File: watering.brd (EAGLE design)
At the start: 84.8 x 64.8 mm, 36 parts, among them IC1 LM324N, IC2 7805T, J1 DCJ0202, Q1 IRF510, T1 2N2222, T2 2N2222, T3 2N2222

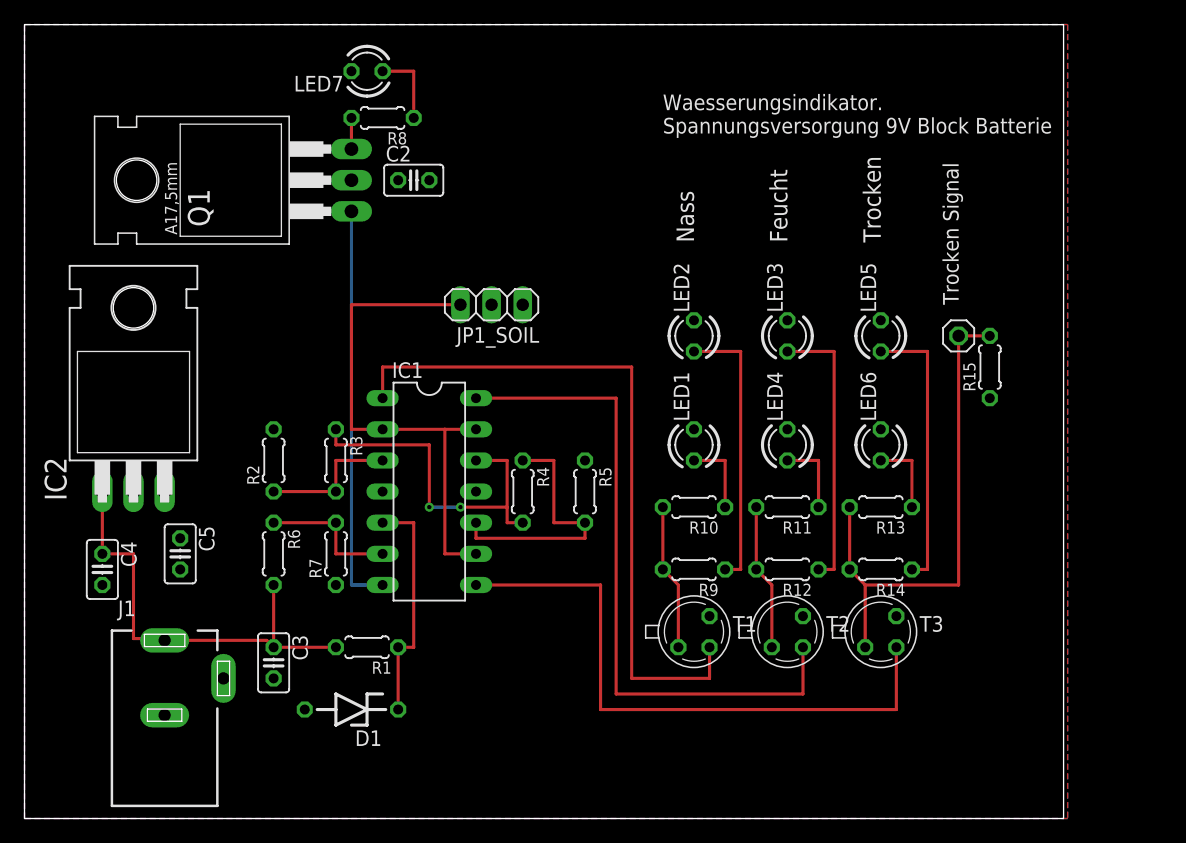
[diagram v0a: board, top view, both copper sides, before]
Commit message: Remove LED labels and reorganised battery indicator to shrinken the design.
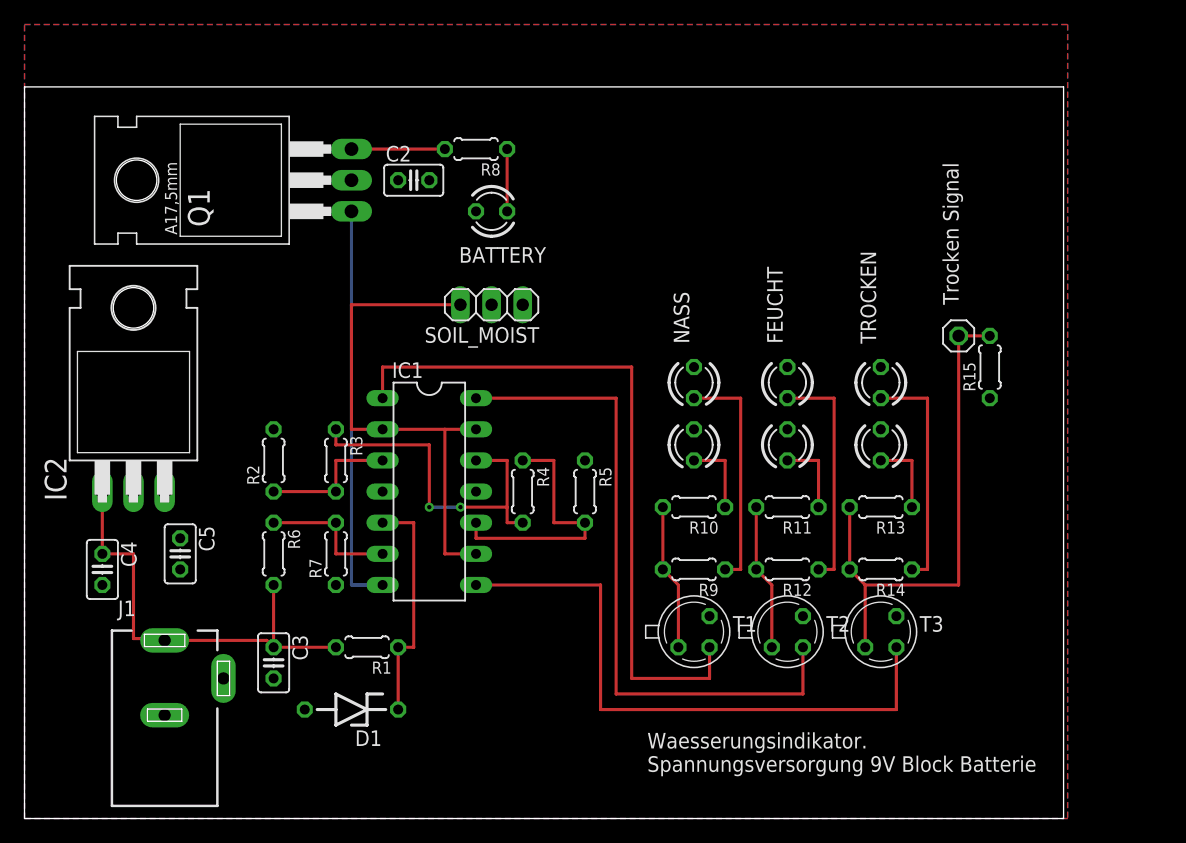
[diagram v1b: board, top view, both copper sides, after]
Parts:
- removed LED2, LED3, LED5, LED7: (no value), led:LED3MM
- added BATTERY, FEUCHT, NASS, TROCKEN: (no value), led:LED3MM
- moved R8 8.03 mm to (34.3, 54.6)
- renumbered JP1_SOIL to SOIL_MOIST
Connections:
- net GND: now also BATTERY.K, FEUCHT.K, NASS.K, TROCKEN.K; no longer LED2.K, LED3.K, LED5.K, LED7.K
- net N$13: now also NASS.A; no longer LED2.A
- net N$21: now also FEUCHT.A; no longer LED3.A
- net N$23: now also TROCKEN.A; no longer LED5.A
- net N$9: now also BATTERY.A; no longer LED7.A
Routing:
- net N$8: track 2.54 -> 7.62 mm
- net N$23: track 22.9 -> 19.1 mm
- net N$21: track 22.9 -> 19.1 mm
- net N$13: track 22.9 -> 19.1 mm
- net N$9: track 6.35 -> 5.08 mm
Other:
- board size 84.8 x 64.8 mm -> 84.8 x 59.7 mm
- board text removed: "Feucht"
- board text removed: "Nass"
- board text removed: "Trocken"
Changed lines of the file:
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@@
 <setting verticaltext="up"/>
 </settings>
-<grid distance="50" unitdist="mil" unit="mil" style="lines" multiple="1" display="no" altdistance="5" altunitdist="mil" altunit="mil"/>
+<grid distance="50" unitdist="mil" unit="mil" style="lines" multiple="1" display="yes" altdistance="5" altunitdist="mil" altunit="mil"/>
 <layers>
 <layer number="1" name="Top" color="4" fill="1" visible="yes" active="yes"/>
@@
 <plain>
 <wire x1="-2.54" y1="0" x2="82.22" y2="0" width="0" layer="20"/>
-<wire x1="82.22" y1="0" x2="82.22" y2="64.76" width="0" layer="20"/>
-<wire x1="82.22" y1="64.76" x2="-2.54" y2="64.76" width="0" layer="20"/>
-<wire x1="-2.54" y1="64.76" x2="-2.54" y2="0" width="0" layer="20"/>
-<text x="52.07" y="46.99" size="1.4224" layer="21" rot="R90">Nass</text>
-<text x="59.69" y="46.99" size="1.4224" layer="21" rot="R90">Feucht</text>
-<text x="67.31" y="46.99" size="1.4224" layer="21" rot="R90">Trocken</text>
-<text x="49.53" y="55.88" size="1.27" layer="21">Waesserungsindikator.
+<wire x1="82.22" y1="0" x2="82.22" y2="59.68" width="0" layer="20"/>
+<wire x1="82.22" y1="59.68" x2="-2.54" y2="59.68" width="0" layer="20"/>
+<wire x1="-2.54" y1="59.68" x2="-2.54" y2="0" width="0" layer="20"/>
+<text x="48.26" y="3.81" size="1.27" layer="21">Waesserungsindikator.
 Spannungsversorgung 9V Block Batterie</text>
 <text x="73.66" y="41.91" size="1.27" layer="21" rot="R90">Trocken Signal</text>
-<dimension x1="-2.54" y1="0" x2="-2.54" y2="64.77" x3="-8.89" y3="32.385" textsize="1.27" layer="1" visible="yes"/>
-<dimension x1="-2.54" y1="64.77" x2="82.55" y2="64.77" x3="40.005" y3="69.85" textsize="1.27" layer="1" visible="yes"/>
+<dimension x1="-2.54" y1="64.77" x2="82.55" y2="64.77" x3="40.005" y3="62.23" textsize="1.27" layer="1" visible="yes"/>
+<dimension x1="-3.81" y1="0" x2="-3.81" y2="59.69" x3="-7.62" y3="29.845" textsize="1.27" layer="1" visible="yes"/>
 </plain>
 <attributes>
@@
 <attribute name="OC_NEWARK" value="unknown" x="8.89" y="11.43" size="1.778" layer="27" display="off"/>
 </element>
-<element name="JP1_SOIL" library="pinhead" package="1X03" value="" x="35.56" y="41.91" rot="R180"/>
-<element name="LED1" library="led" package="LED3MM" value="" x="52.07" y="30.48" rot="R90"/>
-<element name="LED2" library="led" package="LED3MM" value="" x="52.07" y="39.37" rot="R90"/>
-<element name="LED3" library="led" package="LED3MM" value="" x="59.69" y="39.37" rot="R90"/>
-<element name="LED4" library="led" package="LED3MM" value="" x="59.69" y="30.48" rot="R90"/>
-<element name="LED5" library="led" package="LED3MM" value="" x="67.31" y="39.37" rot="R90"/>
-<element name="LED6" library="led" package="LED3MM" value="" x="67.31" y="30.48" rot="R90"/>
+<element name="SOIL_MOIST" library="pinhead" package="1X03" value="" x="35.56" y="41.91" smashed="yes" rot="R180">
+<attribute name="NAME" x="39.4462" y="40.0812" size="1.27" layer="25" ratio="10" rot="R180"/>
+<attribute name="VALUE" x="39.37" y="45.085" size="1.27" layer="27" rot="R180"/>
+</element>
+<element name="LED1" library="led" package="LED3MM" value="" x="52.07" y="30.48" smashed="yes" rot="R90">
+<attribute name="VALUE" x="53.721" y="32.385" size="1.27" layer="27" ratio="10" rot="R90"/>
+</element>
+<element name="NASS" library="led" package="LED3MM" value="" x="52.07" y="35.56" smashed="yes" rot="R90">
+<attribute name="NAME" x="51.689" y="38.735" size="1.27" layer="25" ratio="10" rot="R90"/>
+<attribute name="VALUE" x="53.721" y="37.465" size="1.27" layer="27" ratio="10" rot="R90"/>
+</element>
+<element name="FEUCHT" library="led" package="LED3MM" value="" x="59.69" y="35.56" smashed="yes" rot="R90">
+<attribute name="NAME" x="59.309" y="38.735" size="1.27" layer="25" ratio="10" rot="R90"/>
+<attribute name="VALUE" x="61.341" y="37.465" size="1.27" layer="27" ratio="10" rot="R90"/>
+</element>
+<element name="LED4" library="led" package="LED3MM" value="" x="59.69" y="30.48" smashed="yes" rot="R90">
+<attribute name="VALUE" x="61.341" y="32.385" size="1.27" layer="27" ratio="10" rot="R90"/>
+</element>
+<element name="TROCKEN" library="led" package="LED3MM" value="" x="67.31" y="35.56" smashed="yes" rot="R90">
+<attribute name="NAME" x="66.929" y="38.735" size="1.27" layer="25" ratio="10" rot="R90"/>
+<attribute name="VALUE" x="68.961" y="37.465" size="1.27" layer="27" ratio="10" rot="R90"/>
+</element>
+<element name="LED6" library="led" package="LED3MM" value="" x="67.31" y="30.48" smashed="yes" rot="R90">
+<attribute name="VALUE" x="68.961" y="32.385" size="1.27" layer="27" ratio="10" rot="R90"/>
+</element>
 <element name="R10" library="resistor" package="0204/5" value="150" x="52.07" y="25.4" rot="R180"/>
 <element name="R11" library="resistor" package="0204/5" value="150" x="59.69" y="25.4" rot="R180"/>
@@
 <element name="R7" library="resistor" package="0204/5" value="10k" x="22.86" y="21.59" rot="R90"/>
 <element name="Q1" library="transistor-fet" package="TO220" value="IRF510" x="17.78" y="52.07" rot="R90"/>
-<element name="R8" library="resistor" package="0204/5" value="220" x="26.67" y="57.15" rot="R180"/>
-<element name="LED7" library="led" package="LED3MM" value="" x="25.4" y="60.96" rot="R180"/>
+<element name="R8" library="resistor" package="0204/5" value="220" x="34.29" y="54.61" rot="R180"/>
+<element name="BATTERY" library="led" package="LED3MM" value="" x="35.56" y="49.53" smashed="yes" rot="R180">
+<attribute name="NAME" x="40.005" y="46.609" size="1.27" layer="25" ratio="10" rot="R180"/>
+<attribute name="VALUE" x="33.655" y="51.181" size="1.27" layer="27" ratio="10" rot="R180"/>
+</element>
 <element name="C3" library="rcl" package="C025-025X050" value="0.1uF" x="17.78" y="12.7" rot="R270"/>
 <element name="JP1" library="pinhead" package="1X01" value="JP2_DSIG" x="73.66" y="39.37" smashed="yes" rot="R90"/>
@@
 <signal name="GND">
 <contactref element="IC1" pad="11"/>
-<contactref element="JP1_SOIL" pad="2"/>
+<contactref element="SOIL_MOIST" pad="2"/>
 <contactref element="C2" pad="2"/>
 <contactref element="R5" pad="1"/>
 <contactref element="LED1" pad="K"/>
-<contactref element="LED2" pad="K"/>
-<contactref element="LED3" pad="K"/>
+<contactref element="NASS" pad="K"/>
+<contactref element="FEUCHT" pad="K"/>
 <contactref element="LED4" pad="K"/>
-<contactref element="LED5" pad="K"/>
+<contactref element="TROCKEN" pad="K"/>
 <contactref element="LED6" pad="K"/>
 <contactref element="J1" pad="2"/>
@@
 <contactref element="D1" pad="A"/>
 <contactref element="R7" pad="1"/>
-<contactref element="LED7" pad="K"/>
+<contactref element="BATTERY" pad="K"/>
 <contactref element="C3" pad="2"/>
 <contactref element="R15" pad="1"/>
@@
 </signal>
 <signal name="SOIL_IN">
-<contactref element="JP1_SOIL" pad="3"/>
+<contactref element="SOIL_MOIST" pad="3"/>
 <contactref element="IC1" pad="2"/>
 <contactref element="IC1" pad="13"/>
@@
 <signal name="N$13">
 <contactref element="R9" pad="1"/>
-<contactref element="LED2" pad="A"/>
+<contactref element="NASS" pad="A"/>
 <wire x1="54.61" y1="20.32" x2="55.88" y2="20.32" width="0.254" layer="1"/>
-<wire x1="55.88" y1="20.32" x2="55.88" y2="38.1" width="0.254" layer="1"/>
-<wire x1="55.88" y1="38.1" x2="52.07" y2="38.1" width="0.254" layer="1"/>
+<wire x1="55.88" y1="20.32" x2="55.88" y2="34.29" width="0.254" layer="1"/>
+<wire x1="55.88" y1="34.29" x2="52.07" y2="34.29" width="0.254" layer="1"/>
 </signal>
 <signal name="N$14">
@@
 <signal name="N$21">
 <contactref element="R12" pad="1"/>
-<contactref element="LED3" pad="A"/>
+<contactref element="FEUCHT" pad="A"/>
 <wire x1="62.23" y1="20.32" x2="63.5" y2="20.32" width="0.254" layer="1"/>
-<wire x1="63.5" y1="20.32" x2="63.5" y2="38.1" width="0.254" layer="1"/>
-<wire x1="63.5" y1="38.1" x2="59.69" y2="38.1" width="0.254" layer="1"/>
+<wire x1="63.5" y1="20.32" x2="63.5" y2="34.29" width="0.254" layer="1"/>
+<wire x1="63.5" y1="34.29" x2="59.69" y2="34.29" width="0.254" layer="1"/>
 </signal>
 <signal name="N$22">
@@
 <signal name="N$23">
 <contactref element="R14" pad="1"/>
-<contactref element="LED5" pad="A"/>
+<contactref element="TROCKEN" pad="A"/>
 <wire x1="69.85" y1="20.32" x2="71.12" y2="20.32" width="0.254" layer="1"/>
-<wire x1="71.12" y1="20.32" x2="71.12" y2="38.1" width="0.254" layer="1"/>
-<wire x1="71.12" y1="38.1" x2="67.31" y2="38.1" width="0.254" layer="1"/>
+<wire x1="71.12" y1="20.32" x2="71.12" y2="34.29" width="0.254" layer="1"/>
+<wire x1="71.12" y1="34.29" x2="67.31" y2="34.29" width="0.254" layer="1"/>
 </signal>
 <signal name="N$24">
@@
 <contactref element="IC2" pad="3"/>
 <contactref element="C5" pad="1"/>
-<contactref element="JP1_SOIL" pad="1"/>
+<contactref element="SOIL_MOIST" pad="1"/>
 <contactref element="C2" pad="1"/>
 <contactref element="IC1" pad="4"/>
@@
 <contactref element="Q1" pad="3"/>
 <contactref element="R8" pad="2"/>
-<wire x1="24.13" y1="54.61" x2="24.13" y2="57.15" width="0.254" layer="1"/>
+<wire x1="24.13" y1="54.61" x2="31.75" y2="54.61" width="0.254" layer="1"/>
 </signal>
 <signal name="N$9">
 <contactref element="R8" pad="1"/>
-<contactref element="LED7" pad="A"/>
-<wire x1="29.21" y1="57.15" x2="29.21" y2="60.96" width="0.254" layer="1"/>
-<wire x1="29.21" y1="60.96" x2="26.67" y2="60.96" width="0.254" layer="1"/>
+<contactref element="BATTERY" pad="A"/>
+<wire x1="36.83" y1="54.61" x2="36.83" y2="49.53" width="0.254" layer="1"/>
 </signal>
 </signals>

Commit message: Update positions and labels for silkscreen
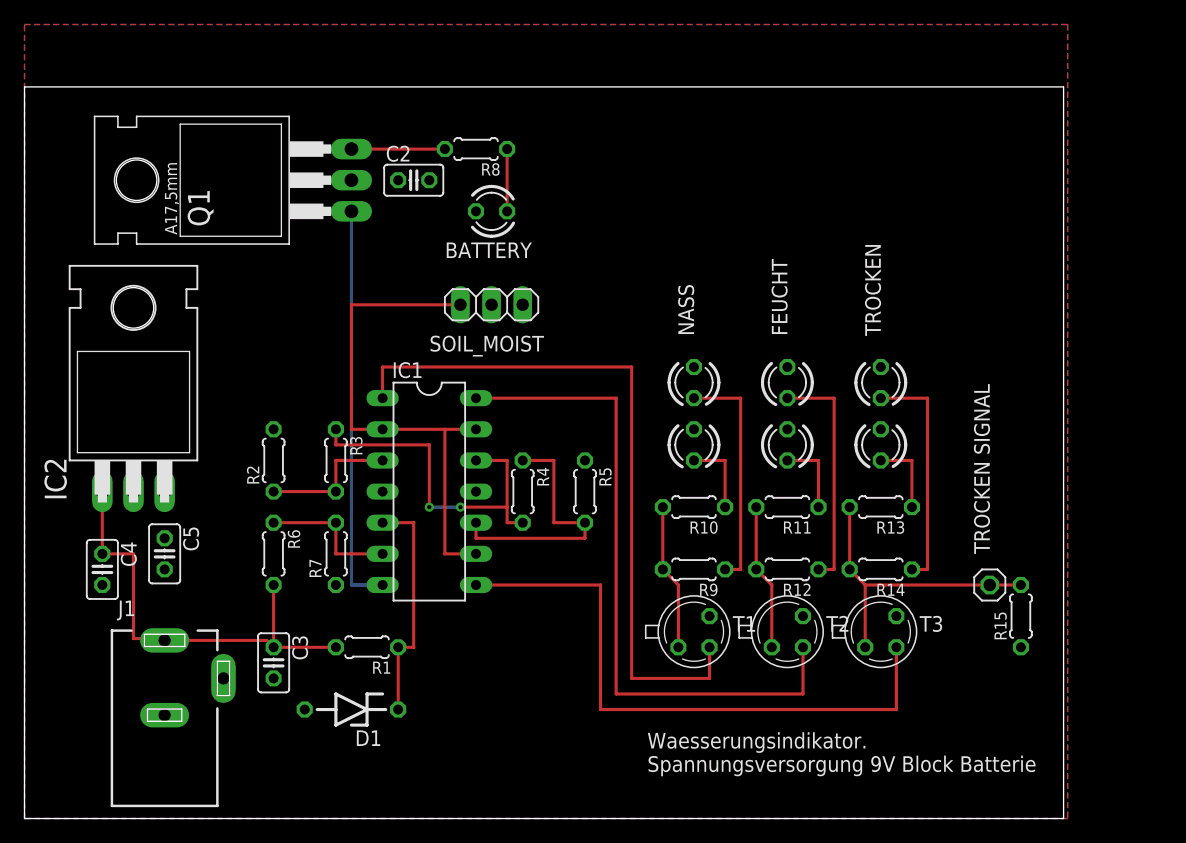
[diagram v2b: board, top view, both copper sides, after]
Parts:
- moved JP1 20.5 mm to (76.2, 19.1)
- moved R15 20.5 mm to (78.7, 16.5)
- moved C5 1.27 mm to (8.89, 21.6)
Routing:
- net N$18: track 42.4 -> 24.7 mm
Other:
- board text added: "BATTERY"
- board text added: "FEUCHT"
- board text added: "NASS"
- board text added: "SOIL_MOIST"
- board text added: "TROCKEN"
- board text added: "TROCKEN SIGNAL"
- board text removed: "Trocken Signal"
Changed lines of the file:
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@@
 <text x="48.26" y="3.81" size="1.27" layer="21">Waesserungsindikator.
 Spannungsversorgung 9V Block Batterie</text>
-<text x="73.66" y="41.91" size="1.27" layer="21" rot="R90">Trocken Signal</text>
+<text x="76.2" y="21.59" size="1.27" layer="21" rot="R90">TROCKEN SIGNAL</text>
 <dimension x1="-2.54" y1="64.77" x2="82.55" y2="64.77" x3="40.005" y3="62.23" textsize="1.27" layer="1" visible="yes"/>
 <dimension x1="-3.81" y1="0" x2="-3.81" y2="59.69" x3="-7.62" y3="29.845" textsize="1.27" layer="1" visible="yes"/>
+<text x="30.48" y="38.1" size="1.27" layer="21">SOIL_MOIST</text>
+<text x="31.75" y="45.72" size="1.27" layer="21">BATTERY</text>
+<text x="52.07" y="39.37" size="1.27" layer="21" rot="R90">NASS</text>
+<text x="59.69" y="39.37" size="1.27" layer="21" rot="R90">FEUCHT</text>
+<text x="67.31" y="39.37" size="1.27" layer="21" rot="R90">TROCKEN</text>
 </plain>
 <attributes>
@@
 <element name="C2" library="rcl" package="C025-025X050" value="0.1uF" x="29.21" y="52.07"/>
 <element name="C4" library="rcl" package="C025-025X050" value="0.22uF" x="3.81" y="20.32" rot="R270"/>
-<element name="C5" library="rcl" package="C025-025X050" value="0.1uF" x="10.16" y="21.59" rot="R270"/>
+<element name="C5" library="rcl" package="C025-025X050" value="0.1uF" x="8.89" y="21.59" rot="R270"/>
 <element name="IC1" library="linear" package="DIL14" value="LM324N" x="30.48" y="26.67" rot="R270"/>
 <element name="IC2" library="linear" package="TO220H" value="7805T" x="6.35" y="36.83"/>
@@
 </element>
 <element name="SOIL_MOIST" library="pinhead" package="1X03" value="" x="35.56" y="41.91" smashed="yes" rot="R180">
-<attribute name="NAME" x="39.4462" y="40.0812" size="1.27" layer="25" ratio="10" rot="R180"/>
 <attribute name="VALUE" x="39.37" y="45.085" size="1.27" layer="27" rot="R180"/>
 </element>
@@
 </element>
 <element name="NASS" library="led" package="LED3MM" value="" x="52.07" y="35.56" smashed="yes" rot="R90">
-<attribute name="NAME" x="51.689" y="38.735" size="1.27" layer="25" ratio="10" rot="R90"/>
 <attribute name="VALUE" x="53.721" y="37.465" size="1.27" layer="27" ratio="10" rot="R90"/>
 </element>
 <element name="FEUCHT" library="led" package="LED3MM" value="" x="59.69" y="35.56" smashed="yes" rot="R90">
-<attribute name="NAME" x="59.309" y="38.735" size="1.27" layer="25" ratio="10" rot="R90"/>
 <attribute name="VALUE" x="61.341" y="37.465" size="1.27" layer="27" ratio="10" rot="R90"/>
 </element>
@@
 </element>
 <element name="TROCKEN" library="led" package="LED3MM" value="" x="67.31" y="35.56" smashed="yes" rot="R90">
-<attribute name="NAME" x="66.929" y="38.735" size="1.27" layer="25" ratio="10" rot="R90"/>
 <attribute name="VALUE" x="68.961" y="37.465" size="1.27" layer="27" ratio="10" rot="R90"/>
 </element>
@@
 <element name="R8" library="resistor" package="0204/5" value="220" x="34.29" y="54.61" rot="R180"/>
 <element name="BATTERY" library="led" package="LED3MM" value="" x="35.56" y="49.53" smashed="yes" rot="R180">
-<attribute name="NAME" x="40.005" y="46.609" size="1.27" layer="25" ratio="10" rot="R180"/>
 <attribute name="VALUE" x="33.655" y="51.181" size="1.27" layer="27" ratio="10" rot="R180"/>
 </element>
 <element name="C3" library="rcl" package="C025-025X050" value="0.1uF" x="17.78" y="12.7" rot="R270"/>
-<element name="JP1" library="pinhead" package="1X01" value="JP2_DSIG" x="73.66" y="39.37" smashed="yes" rot="R90"/>
-<element name="R15" library="resistor" package="0204/5" value="4.7k" x="76.2" y="36.83" rot="R90"/>
+<element name="JP1" library="pinhead" package="1X01" value="JP2_DSIG" x="76.2" y="19.05" smashed="yes" rot="R90"/>
+<element name="R15" library="resistor" package="0204/5" value="4.7k" x="78.74" y="16.51" rot="R90"/>
 </elements>
 <signals>
@@
 <contactref element="JP1" pad="1"/>
 <contactref element="R15" pad="2"/>
-<wire x1="73.66" y1="39.37" x2="76.2" y2="39.37" width="0.254" layer="1"/>
-<wire x1="66.04" y1="19.05" x2="73.66" y2="19.05" width="0.254" layer="1"/>
-<wire x1="73.66" y1="19.05" x2="73.66" y2="39.37" width="0.254" layer="1"/>
+<wire x1="76.2" y1="19.05" x2="78.74" y2="19.05" width="0.254" layer="1"/>
+<wire x1="66.04" y1="19.05" x2="76.2" y2="19.05" width="0.254" layer="1"/>
 </signal>
 <signal name="N$21">

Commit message: Update parts and pcb image
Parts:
- T3: value 2N2222 -> 2N2222A; device transistor:TO18 -> transistor-npn:TO18
- moved SOIL_MOIST 14.9 mm to (21.6, 36.8), turned to 270 degrees
- moved BATTERY 10.2 mm to (44.5, 44.5)
- moved C2 10.2 mm to (38.1, 47.0)
- moved Q1 10.2 mm to (26.7, 47.0)
- moved R8 10.2 mm to (43.2, 49.5)
- moved R5 2.54 mm to (40.6, 26.7)
- turned R4 to 90 degrees
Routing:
- net N$11: track 29.2 -> 49.5 mm, vias 2 -> 0
- net SOIL_IN: track 43.2 -> 29.2 mm
- net N$12: track 21.6 -> 11.4 mm
- net N$7: track 33.0 -> 36.8 mm
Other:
- board size 84.8 x 59.7 mm -> 84.8 x 54.6 mm
- board text added: "+9V SUPPLY"
